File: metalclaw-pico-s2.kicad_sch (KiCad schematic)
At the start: 54 parts, among them J1 USB_C_Receptacle_USB2.0_14P, U1 ESP32-S2, U2 MX25L3236FM2I-08G-TR, U3 APS6404L-3SQRx-SN, U5 XC6220B331MR, Y1 XRCGB40M000F1S2FR0

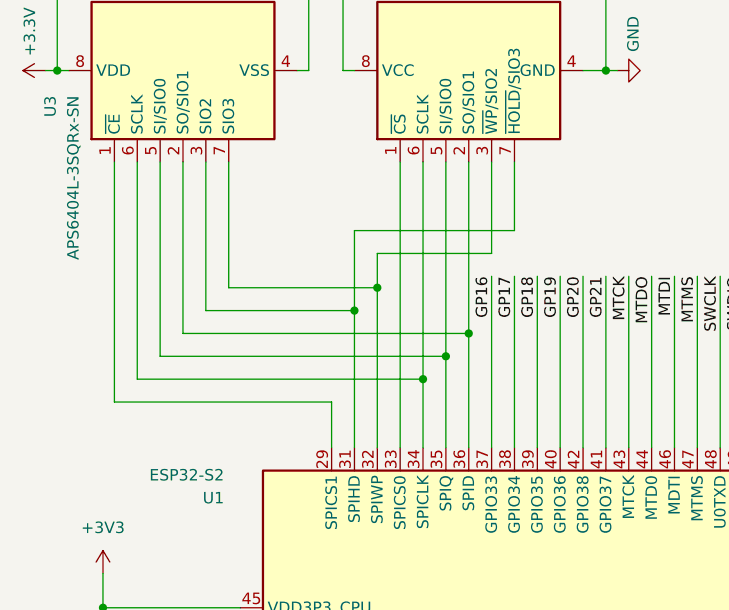
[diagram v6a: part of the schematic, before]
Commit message: Swap SPID and SPIQ wiring to PSRAM and flash chips
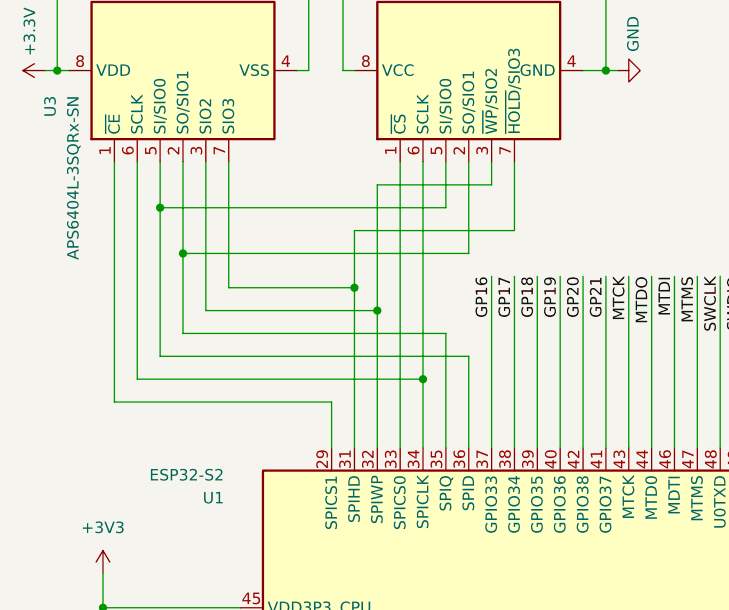
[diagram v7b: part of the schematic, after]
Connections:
- net at U2.2 (SO/SIO1), U3.2 (SO/SIO1): now also U1.35 (SPIQ); no longer U1.36 (SPID)
- net at U1.32 (SPIWP), U2.3 (~{WP}/SIO2): now also U3.3 (SIO2); no longer U3.7 (SIO3)
- net at U2.5 (SI/SIO0), U3.5 (SI/SIO0): now also U1.36 (SPID); no longer U1.35 (SPIQ)
- net at U1.31 (SPIHD), U2.7 (~{HOLD}/SIO3): now also U3.7 (SIO3); no longer U3.3 (SIO2)
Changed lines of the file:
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@@
-	)
-	(junction
-		(at 88.9 72.39)
-		(diameter 0)
-		(color 0 0 0 0)
 	)
 	(junction
@@
 	)
 	(junction
-		(at 76.2 69.85)
-		(diameter 0)
-		(color 0 0 0 0)
-	)
-	(junction
 		(at 121.92 60.96)
 		(diameter 0)
@@
 	)
 	(junction
-		(at 86.36 74.93)
-		(diameter 0)
-		(color 0 0 0 0)
-	)
-	(junction
 		(at 151.13 66.04)
 		(diameter 0)
@@
 	)
 	(junction
+		(at 57.15 63.5)
+		(diameter 0)
+		(color 0 0 0 0)
+	)
+	(junction
 		(at 48.26 110.49)
 		(diameter 0)
@@
 	)
 	(junction
-		(at 78.74 67.31)
+		(at 54.61 58.42)
 		(diameter 0)
 		(color 0 0 0 0)
@@
 	)
 	(junction
+		(at 76.2 67.31)
+		(diameter 0)
+		(color 0 0 0 0)
+	)
+	(junction
 		(at 262.89 71.12)
 		(diameter 0)
@@
 	(junction
 		(at 215.9 152.4)
+		(diameter 0)
+		(color 0 0 0 0)
+	)
+	(junction
+		(at 78.74 69.85)
 		(diameter 0)
 		(color 0 0 0 0)
@@
 	(wire
 		(pts
+			(xy 57.15 63.5) (xy 57.15 72.39)
+		)
+		(stroke
+			(width 0)
+			(type default)
+		)
+	)
+	(wire
+		(pts
 			(xy 151.13 107.95) (xy 151.13 133.35)
 		)
@@
 	(wire
 		(pts
-			(xy 91.44 53.34) (xy 91.44 63.5)
+			(xy 91.44 53.34) (xy 91.44 55.88)
 		)
 		(stroke
@@
 	(wire
 		(pts
+			(xy 54.61 74.93) (xy 88.9 74.93)
+		)
+		(stroke
+			(width 0)
+			(type default)
+		)
+	)
+	(wire
+		(pts
 			(xy 240.03 148.59) (xy 240.03 152.4)
 		)
@@
 	(wire
 		(pts
+			(xy 54.61 58.42) (xy 86.36 58.42)
+		)
+		(stroke
+			(width 0)
+			(type default)
+		)
+	)
+	(wire
+		(pts
 			(xy 191.77 71.12) (xy 190.5 71.12)
 		)
@@
 	(wire
 		(pts
-			(xy 57.15 53.34) (xy 57.15 72.39)
+			(xy 57.15 53.34) (xy 57.15 63.5)
 		)
 		(stroke
@@
 	(wire
 		(pts
-			(xy 54.61 53.34) (xy 54.61 74.93)
-		)
-		(stroke
-			(width 0)
-			(type default)
-		)
-	)
-	(wire
-		(pts
-			(xy 88.9 85.09) (xy 88.9 72.39)
+			(xy 54.61 53.34) (xy 54.61 58.42)
 		)
 		(stroke
@@
 	(wire
 		(pts
-			(xy 86.36 85.09) (xy 86.36 74.93)
-		)
-		(stroke
-			(width 0)
-			(type default)
-		)
-	)
-	(wire
-		(pts
 			(xy 83.82 130.81) (xy 83.82 147.32)
 		)
@@
 	(wire
 		(pts
+			(xy 88.9 53.34) (xy 88.9 63.5)
+		)
+		(stroke
+			(width 0)
+			(type default)
+		)
+	)
+	(wire
+		(pts
 			(xy 48.26 113.03) (xy 48.26 115.57)
 		)
@@
 	(wire
 		(pts
-			(xy 88.9 72.39) (xy 88.9 53.34)
-		)
-		(stroke
-			(width 0)
-			(type default)
-		)
-	)
-	(wire
-		(pts
 			(xy 257.81 68.58) (xy 269.24 68.58)
 		)
@@
 	(wire
 		(pts
+			(xy 78.74 69.85) (xy 78.74 85.09)
+		)
+		(stroke
+			(width 0)
+			(type default)
+		)
+	)
+	(wire
+		(pts
 			(xy 114.3 66.04) (xy 114.3 85.09)
 		)
@@
 	(wire
 		(pts
-			(xy 78.74 67.31) (xy 78.74 85.09)
-		)
-		(stroke
-			(width 0)
-			(type default)
-		)
-	)
-	(wire
-		(pts
-			(xy 57.15 72.39) (xy 88.9 72.39)
+			(xy 62.23 67.31) (xy 76.2 67.31)
 		)
 		(stroke
@@
 	(wire
 		(pts
-			(xy 54.61 74.93) (xy 86.36 74.93)
-		)
-		(stroke
-			(width 0)
-			(type default)
-		)
-	)
-	(wire
-		(pts
 			(xy 52.07 77.47) (xy 83.82 77.47)
 		)
@@
 	(wire
 		(pts
-			(xy 78.74 63.5) (xy 78.74 67.31)
+			(xy 78.74 55.88) (xy 78.74 69.85)
 		)
 		(stroke
@@
 	(wire
 		(pts
+			(xy 59.69 69.85) (xy 78.74 69.85)
+		)
+		(stroke
+			(width 0)
+			(type default)
+		)
+	)
+	(wire
+		(pts
 			(xy 138.43 146.05) (xy 140.97 146.05)
 		)
@@
 	(wire
 		(pts
-			(xy 62.23 67.31) (xy 78.74 67.31)
-		)
-		(stroke
-			(width 0)
-			(type default)
-		)
-	)
-	(wire
-		(pts
 			(xy 191.77 86.36) (xy 190.5 86.36)
 		)
@@
 	(wire
 		(pts
+			(xy 54.61 58.42) (xy 54.61 74.93)
+		)
+		(stroke
+			(width 0)
+			(type default)
+		)
+	)
+	(wire
+		(pts
 			(xy 148.59 146.05) (xy 151.13 146.05)
 		)
@@
 	(wire
 		(pts
+			(xy 88.9 63.5) (xy 57.15 63.5)
+		)
+		(stroke
+			(width 0)
+			(type default)
+		)
+	)
+	(wire
+		(pts
 			(xy 48.26 113.03) (xy 63.5 113.03)
 		)
@@
 	(wire
 		(pts
-			(xy 86.36 74.93) (xy 86.36 53.34)
-		)
-		(stroke
-			(width 0)
-			(type default)
-		)
-	)
-	(wire
-		(pts
 			(xy 191.77 73.66) (xy 190.5 73.66)
 		)
@@
 	(wire
 		(pts
-			(xy 76.2 69.85) (xy 76.2 85.09)
+			(xy 76.2 67.31) (xy 76.2 85.09)
 		)
 		(stroke
@@
 	(wire
 		(pts
+			(xy 86.36 53.34) (xy 86.36 58.42)
+		)
+		(stroke
+			(width 0)
+			(type default)
+		)
+	)
+	(wire
+		(pts
 			(xy 52.07 144.78) (xy 48.26 144.78)
 		)
@@
 	(wire
 		(pts
-			(xy 76.2 60.96) (xy 76.2 69.85)
+			(xy 76.2 60.96) (xy 76.2 67.31)
 		)
 		(stroke
@@
 	(wire
 		(pts
-			(xy 59.69 69.85) (xy 76.2 69.85)
-		)
-		(stroke
-			(width 0)
-			(type default)
-		)
-	)
-	(wire
-		(pts
 			(xy 81.28 85.09) (xy 81.28 53.34)
 		)
@@
 	(wire
 		(pts
+			(xy 86.36 72.39) (xy 86.36 85.09)
+		)
+		(stroke
+			(width 0)
+			(type default)
+		)
+	)
+	(wire
+		(pts
 			(xy 104.14 29.21) (xy 104.14 43.18)
 		)
@@
 	(wire
 		(pts
+			(xy 57.15 72.39) (xy 86.36 72.39)
+		)
+		(stroke
+			(width 0)
+			(type default)
+		)
+	)
+	(wire
+		(pts
 			(xy 209.55 33.02) (xy 209.55 31.75)
 		)
@@
 	(wire
 		(pts
-			(xy 91.44 63.5) (xy 78.74 63.5)
+			(xy 91.44 55.88) (xy 78.74 55.88)
 		)
 		(stroke
@@
 		)
 		(stroke
+			(width 0)
+			(type default)
+		)
+	)
+	(wire
+		(pts
+			(xy 88.9 74.93) (xy 88.9 85.09)
+		)
+		(stroke

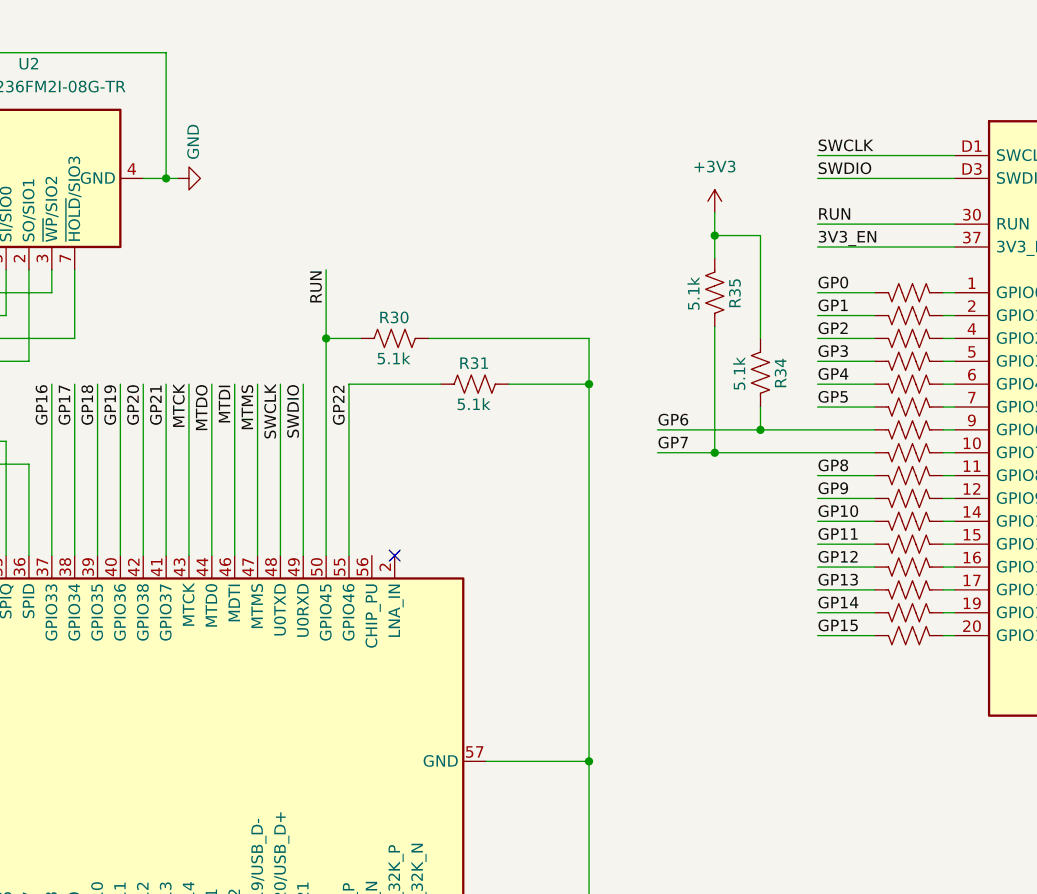
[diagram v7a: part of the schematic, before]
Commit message: Add more I2C pins
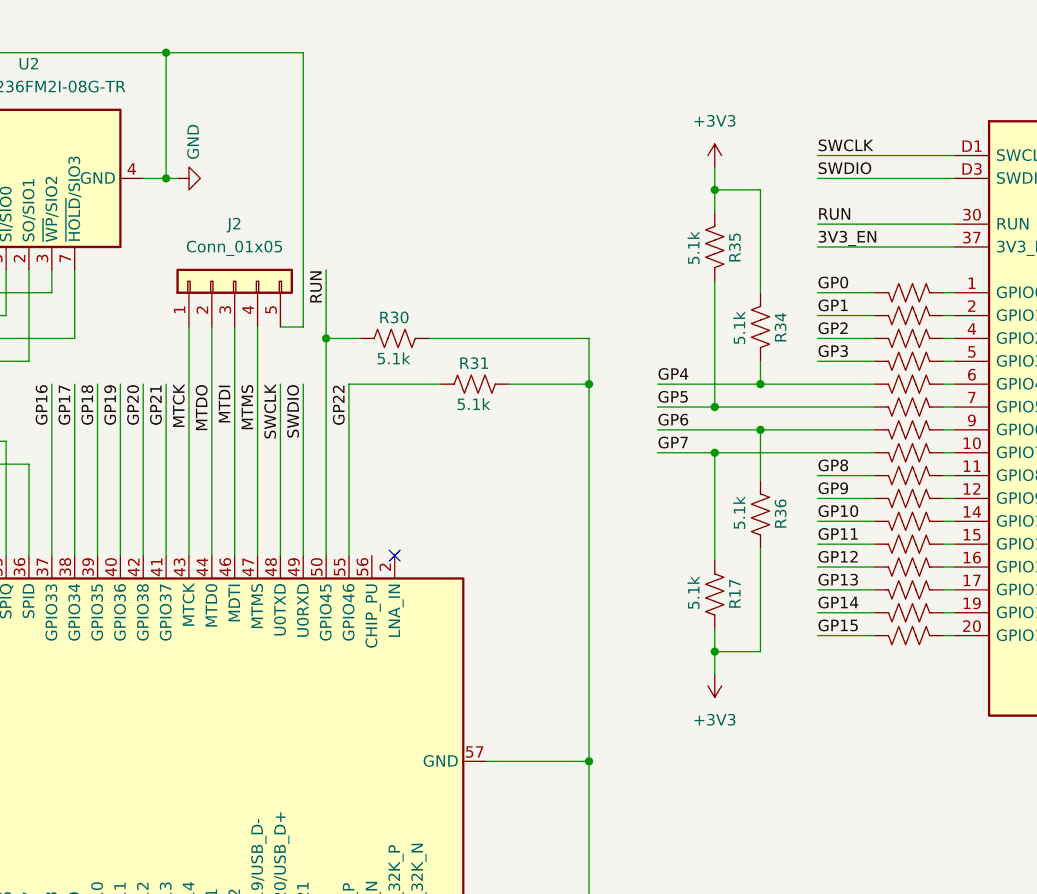
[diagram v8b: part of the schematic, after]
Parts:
- added J2: Conn_01x05, Connector_PinHeader_2.54mm:PinHeader_1x05_P2.54mm_Vertical, symbol Connector_Generic:Conn_01x05
- added R17, R36: 5.1k, Capacitor_SMD:C_0402_1005Metric, symbol Device:R_US
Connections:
- net +3V3: now also R17.1, R36.1
- net GND: now also J2.5 (Pin_5)
- net GP4: now also R34.2
- net GP5: now also R35.2
- net GP6: now also R36.2; no longer R34.2
- net GP7: now also R17.2; no longer R35.2
- net MTCK: now also J2.1 (Pin_1)
- net MTDI: now also J2.3 (Pin_3)
- net MTDO: now also J2.2 (Pin_2)
- net MTMS: now also J2.4 (Pin_4)
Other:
- moved on the sheet: R34, R35
